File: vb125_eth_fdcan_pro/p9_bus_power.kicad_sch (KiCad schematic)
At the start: 12 parts, among them U7 LT8304IS8E#PBF

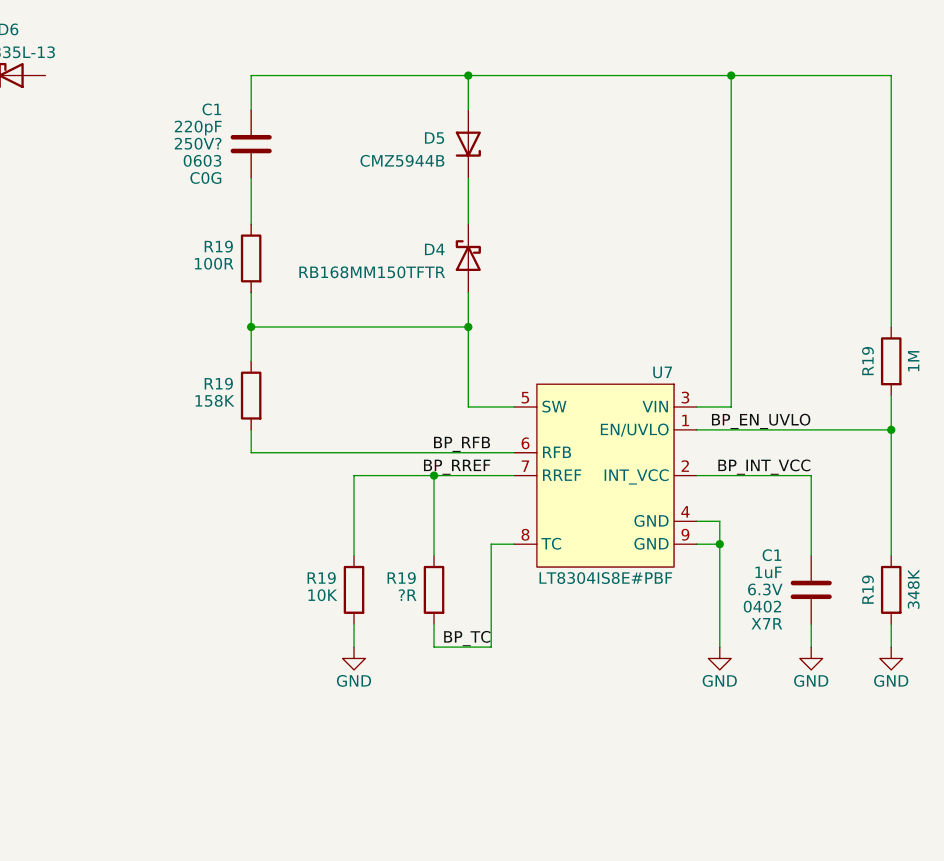
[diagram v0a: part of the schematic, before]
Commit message: Work on PoE. Rearrange pages.
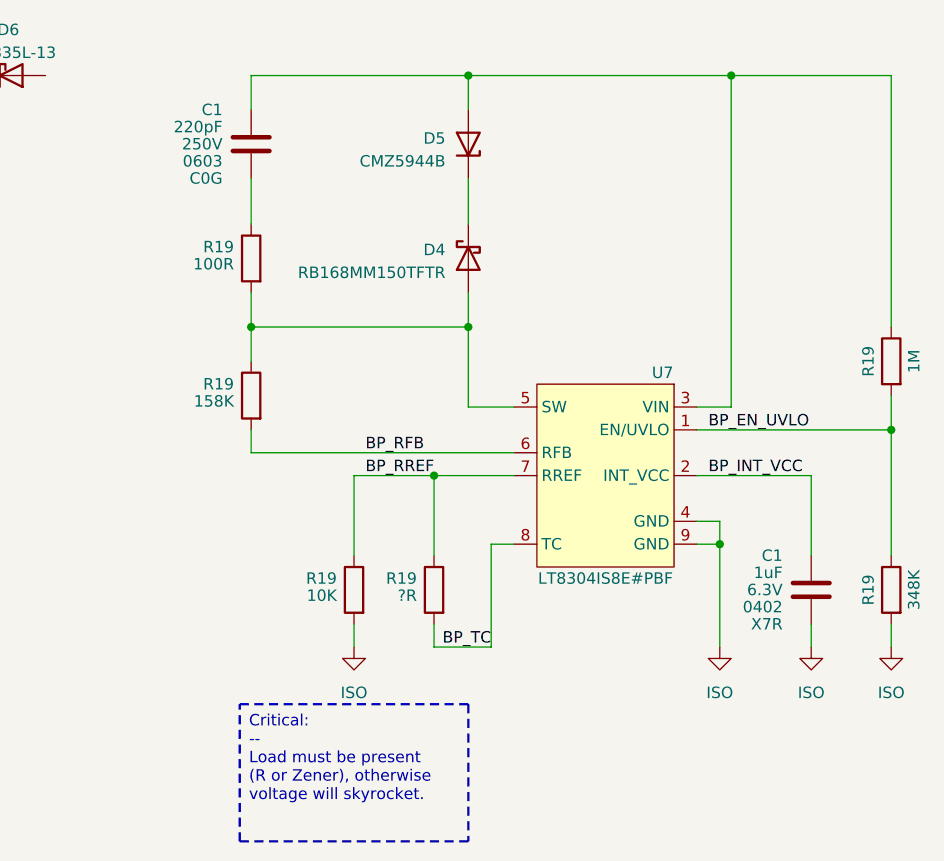
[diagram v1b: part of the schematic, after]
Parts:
- C1: Voltage 250V? -> 250V
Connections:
- net GND renamed ISO

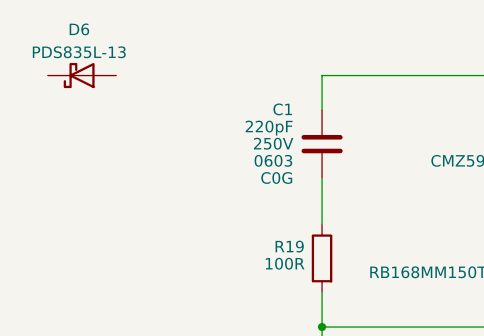
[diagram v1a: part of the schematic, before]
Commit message: Finish PoE schematic.
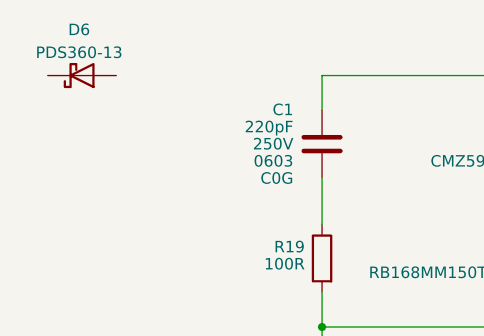
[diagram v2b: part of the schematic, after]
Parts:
- D6: value PDS835L-13 -> PDS360-13
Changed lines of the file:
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@@
       (effects (font (size 1.27 1.27)))
     )
-    (property "Value" "PDS835L-13" (at 110.1725 49.53 0)
+    (property "Value" "PDS360-13" (at 110.1725 49.53 0)
       (effects (font (size 1.27 1.27)))
     )

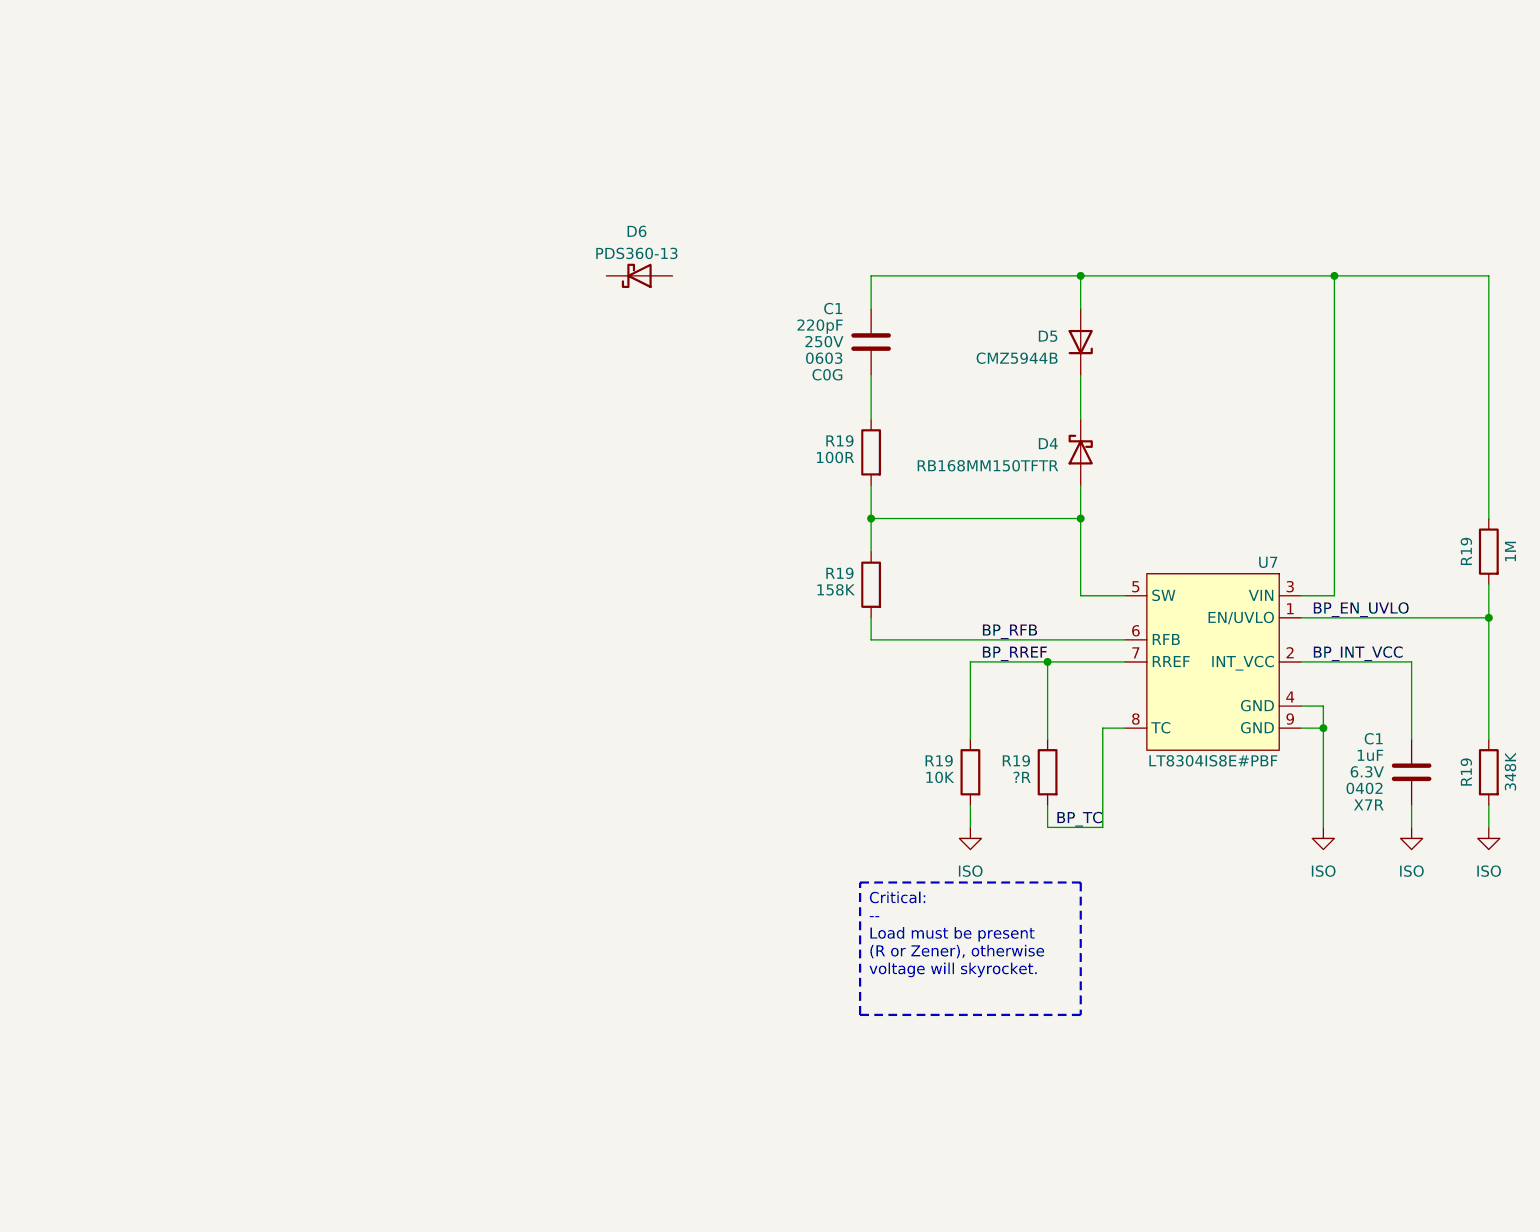
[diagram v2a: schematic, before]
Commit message: CAN schematics. Assign IO on H7.
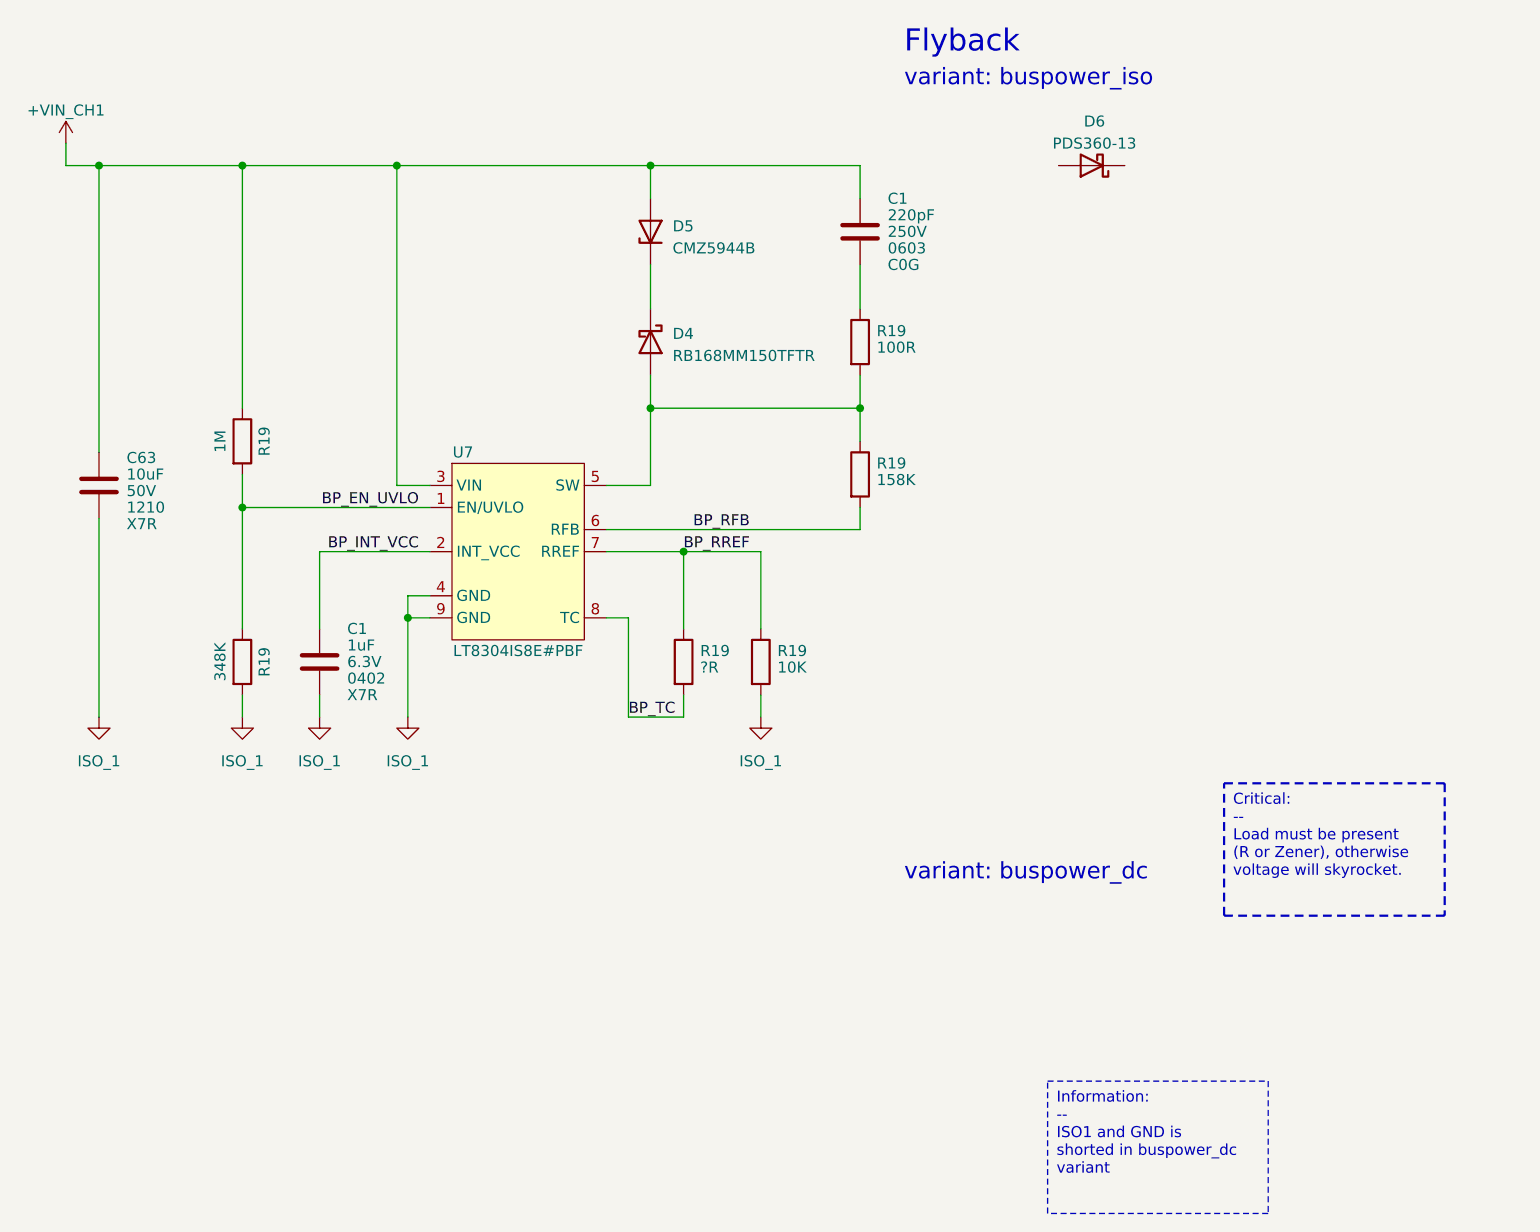
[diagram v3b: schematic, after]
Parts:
- added C63: 10uF, Capacitor_SMD:C_1210_3225Metric, symbol Device:C
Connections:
- net +VIN_CH1: now reaches C1.1, D5.2 (A), R19.1, U7.3 (VIN)
- net +VIN_CH1: now also C63.1
- net ISO renamed ISO_1
- net ISO_1: now also C63.2
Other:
- note added: "Flyback"
- note added: "variant: buspower_dc"
- note added: "variant: buspower_iso"
- moved on the sheet: C1, D4, D5, D6, R19, U7

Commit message: Finish schematics.
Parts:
- added C1, C2, C20: 100nF, Capacitor_SMD:C_0402_1005Metric, symbol Device:C
- added C63 (x4): 4.7uF, Capacitor_SMD:C_1210_3225Metric, symbol Device:C
- added C66 (x4): 100uF, Capacitor_SMD:C_1210_3225Metric, symbol Device:C
- added D20: RB168MM150TFTR, Diode_SMD:D_SOD-123F, symbol Device:D_Schottky
- added D21: buspower_iso: SMAJ58CA; buspower_dc: SMAJ36CA, Diode_SMD:D_SMA, symbol Device:D_TVS
- added D23: PDS360-13, Diode_SMD:D_PowerDI-5, symbol Device:D_Schottky
- added D3: 5V6?, Diode_SMD:D_SOD-323, symbol Device:D_Zener
- added JP1: Jumper board, vhrd_generic:PCB_JUMPER, symbol Jumper:SolderJumper_2_Open
- added L6: LMLP07A7M8R2DTAS, vhrd_inductor:LMLP07A7, symbol Device:L_Iron
- added R19 (x2): 10K, Resistor_SMD:R_0402_1005Metric, symbol Device:R
- added R19: 250R, Resistor_SMD:R_0603_1608Metric, symbol Device:R
- added R19: 57K6, Resistor_SMD:R_0402_1005Metric, symbol Device:R
- added R19: 49K9, Resistor_SMD:R_0402_1005Metric, symbol Device:R
- added T2: 750315125, vhrd_transformer:750315125, symbol vhrd_transformer:750315125
- added U4: LV14360SDDAR, Package_SO:SOIC-8-1EP_3.9x4.9mm_P1.27mm_EP2.95x4.9mm_Mask2.71x3.4mm_ThermalVias, symbol vhrd_pmic_regulator:LV14360SDDAR
- C1: footprint (none) -> Capacitor_SMD:C_0603_1608Metric
- C1: footprint (none) -> Capacitor_SMD:C_0402_1005Metric
- D6: Irated (none) -> 3A; Vrated (none) -> 60V
- R19: now not fitted
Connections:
- net ISO_1: now also C1.2, C2.2, C63.2, C63.2, C63.2, C63.2, C66.2, D23.2 (A), R19.1, R19.2, U4.7 (GND), U4.9 (EPAD_GND)
- net BP_SW: now reaches D4.2 (A), R19.1, R19.2, U7.5 (SW)
- net BP_SW: now also T2.3
- net +5V0_SYS: now reaches D6.1 (K)
- net +5V0_SYS: now also C66.1, C66.1, C66.1, D3.1 (K), JP1.2 (B), R19.1
- net at D6.2 (A): now also T2.6, T2.7
- net +VIN_CH1 renamed +VIN_DB9_PR
- net +VIN_DB9_PR: now also C1.1, C63.1, C63.1, C63.1, C63.1, D20.1 (K), R19.1, T2.5, U4.2 (VIN)
- new net +5V0_BP_DC: C66.1, JP1.1 (A), L6.2, R19.2
- new net +VIN_DB9: D20.2 (A), D21.2 (A2)
- new net CHASSIS: D21.1 (A1)
- new net GND: C66.2, C66.2, C66.2, D3.2 (A), R19.2, T2.10, T2.9
- new net LV_BOOT: C20.1, U4.1 (BOOT)
- new net LV_EN: R19.2, U4.3 (EN)
- new net LV_FB: R19.1, R19.2, U4.5 (FB)
- new net LV_RT: R19.1, U4.4 (RT/SYNC)
- new net LV_SS: C2.1, U4.6 (SS)
- new net LV_SW: C20.2, D23.1 (K), L6.1, U4.8 (SW)
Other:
- note added: "Buck"
- moved on the sheet: C1, C63, D4, D5, D6, R19, U7

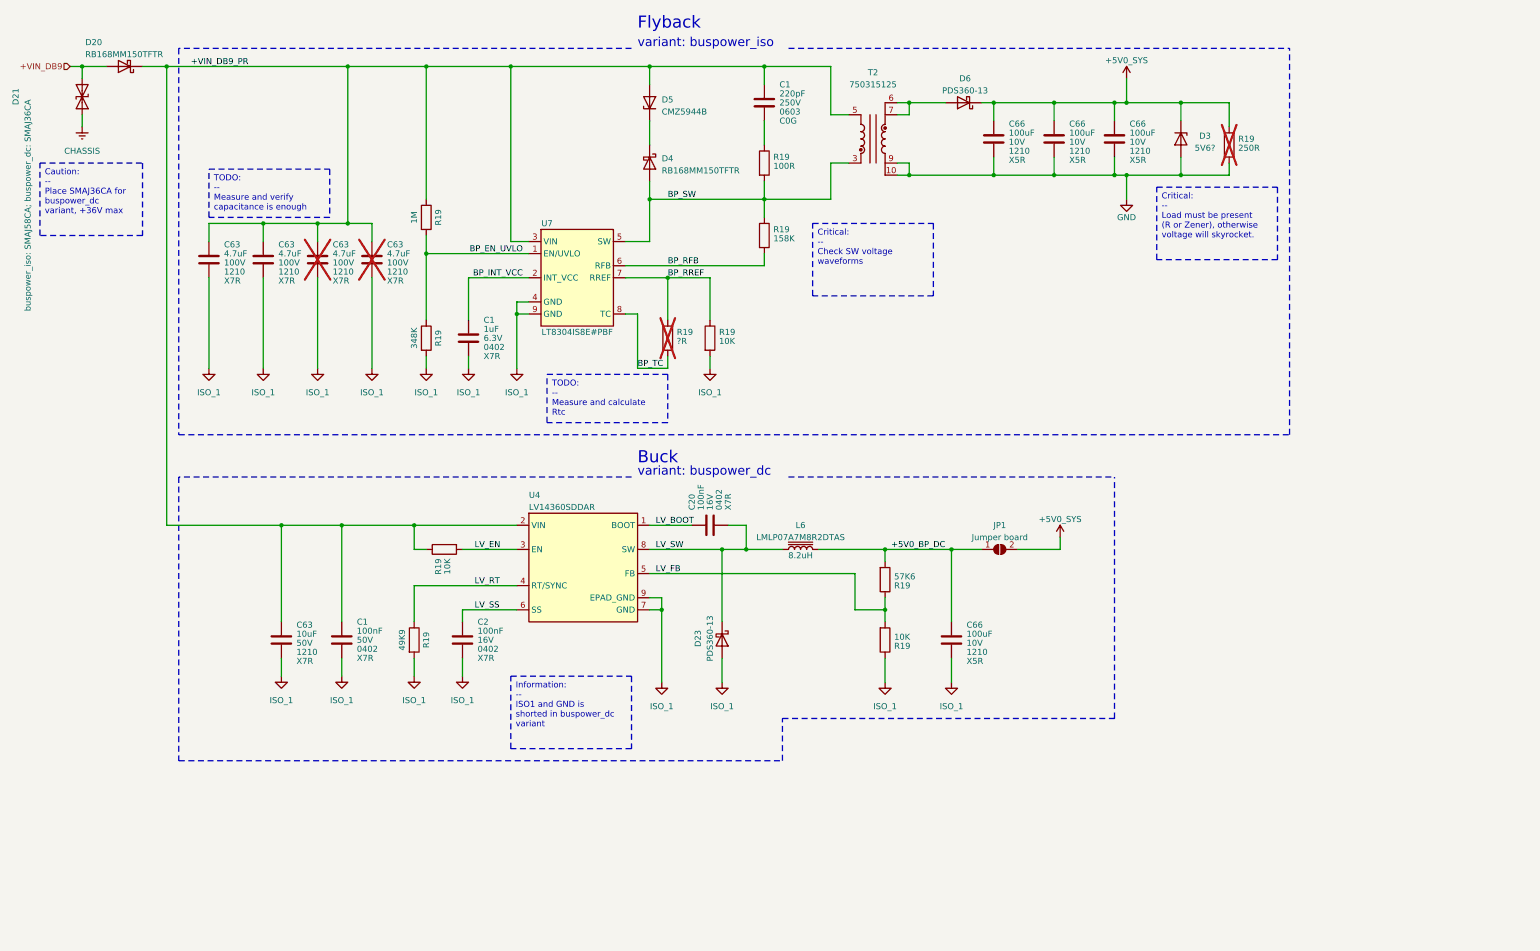
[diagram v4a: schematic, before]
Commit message: Add testpoints and set page templates.
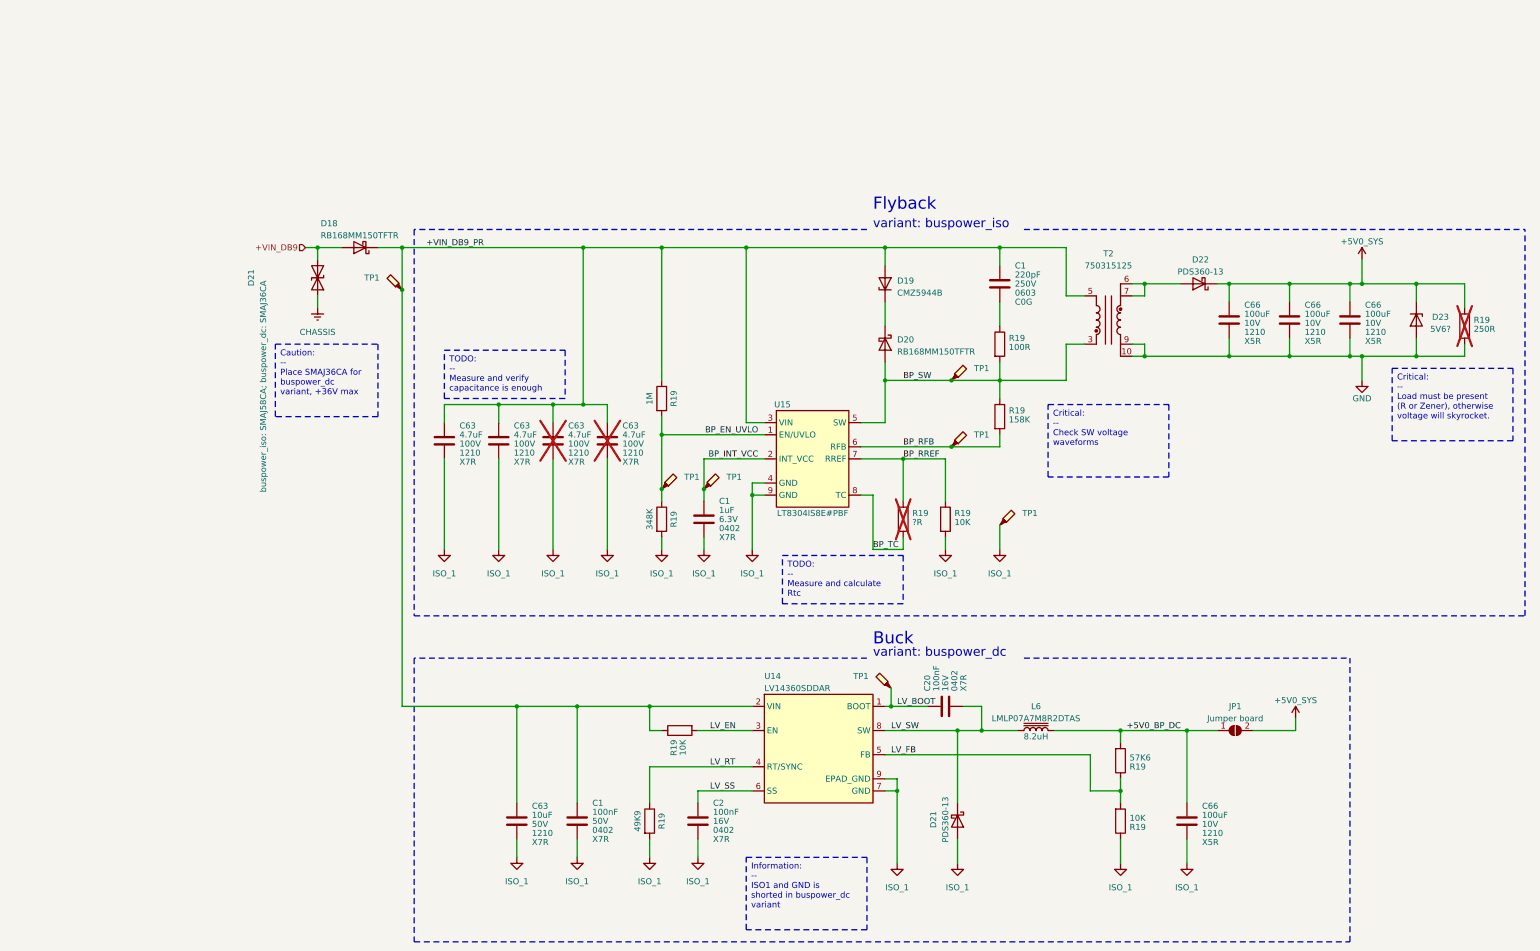
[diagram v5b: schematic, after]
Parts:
- added TP1 (x7): TestPoint_Probe, TestPoint:TestPoint_Pad_D1.5mm, symbol Connector:TestPoint_Probe
- renumbered D20 to D18, D5 to D19, D4 to D20, D23 to D21, D6 to D22, D3 to D23, U4 to U14, U7 to U15
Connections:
- net +VIN_DB9_PR: now also TP1.1
- net BP_EN_UVLO: now also TP1.1
- net BP_INT_VCC: now also TP1.1
- net BP_RFB: now also TP1.1
- net BP_SW: now also TP1.1
- net ISO_1: now also TP1.1
- net LV_BOOT: now also TP1.1
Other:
- company: (none) -> vhrd.tech AS
- title: (none) -> rt_bridge_pro
- moved on the sheet: C1, C2, C20, C63, C66, D18, D19, D20, D21, D22, D23, JP1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
